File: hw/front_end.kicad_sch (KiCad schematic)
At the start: 6 parts, among them Q5 SSM6P35AFE, Q6 SSM6P35AFE

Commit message: WIP - a lot already laid out.
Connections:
- net FE_CHA/PGA_CTL_CLK: now also Q6.3 (D); no longer Q6.6 (D)
- net FE_CHA/PGA_CTL_DATA: now also Q5.6 (D); no longer Q6.3 (D)
- net FE_CHA/PGA_CTL_LATCH: now also Q6.6 (D); no longer Q5.3 (D)
- net FE_CHB/PGA_CTL_LATCH: now also Q5.3 (D); no longer Q5.6 (D)
- net PGA_LATCH_CHA: now also Q6.2 (G); no longer Q5.5 (G)
- net PGA_LATCH_CHB: now also Q5.5 (G); no longer Q5.2 (G)
- net PGA_SCLK: now also Q6.5 (G); no longer Q6.2 (G)
- net PGA_SDAT: now also Q5.2 (G); no longer Q6.5 (G)
- no-connect marks 2 -> 0
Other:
- sheet FE_CHA ports: added PGA_INLO, SE_OUT; removed none
- sheet FE_CHB ports: added PGA_INLO, SE_OUT; removed none
- moved on the sheet: Q5A, Q5B, Q6A, Q6B

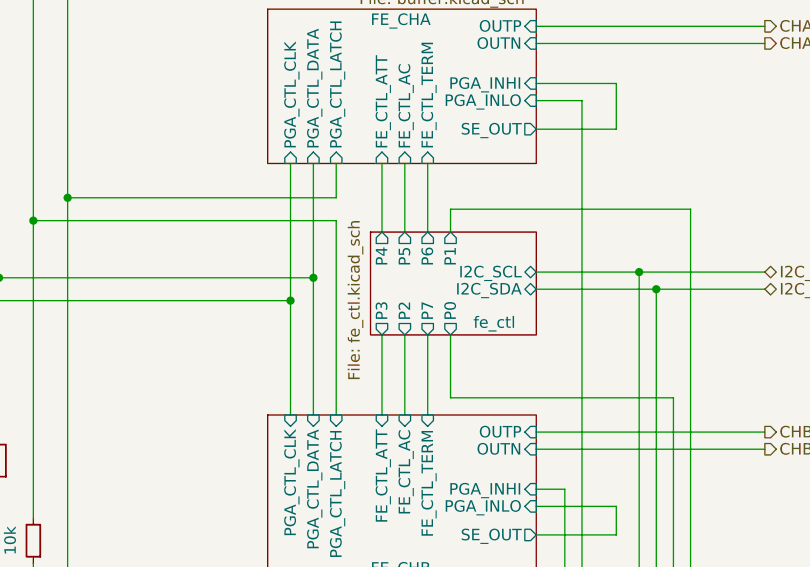
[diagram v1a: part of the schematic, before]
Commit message: WIP - almost everything except power (converters) connected
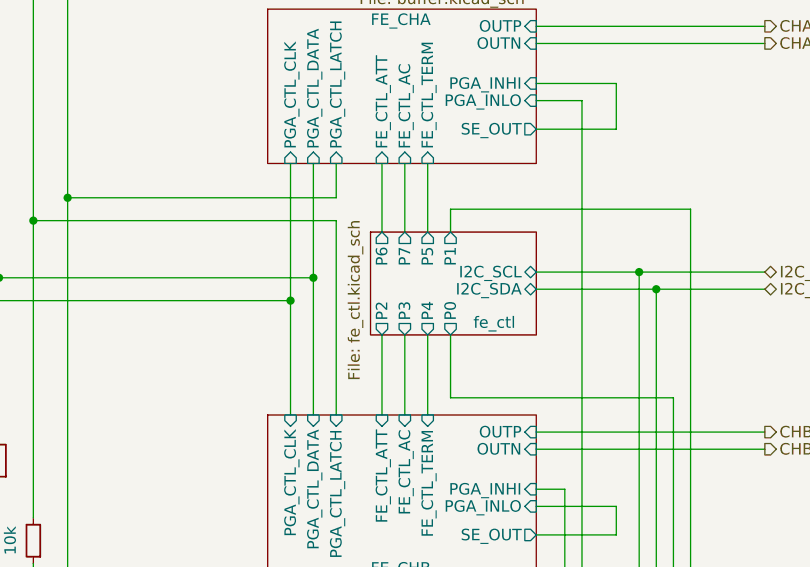
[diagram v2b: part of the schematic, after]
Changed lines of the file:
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@@
       (effects (font (size 1.27 1.27)) (justify left top))
     )
-    (pin "P7" output (at 111.125 113.03 270)
-      (effects (font (size 1.27 1.27)) (justify left))
+    (pin "P7" output (at 108.585 101.6 90)
+      (effects (font (size 1.27 1.27)) (justify right))
     )
     (pin "P0" output (at 113.665 113.03 270)
       (effects (font (size 1.27 1.27)) (justify left))
     )
-    (pin "P6" output (at 111.125 101.6 90)
+    (pin "P6" output (at 106.045 101.6 90)
       (effects (font (size 1.27 1.27)) (justify right))
     )
-    (pin "P5" output (at 108.585 101.6 90)
+    (pin "P5" output (at 111.125 101.6 90)
       (effects (font (size 1.27 1.27)) (justify right))
     )
-    (pin "P4" output (at 106.045 101.6 90)
-      (effects (font (size 1.27 1.27)) (justify right))
+    (pin "P4" output (at 111.125 113.03 270)
+      (effects (font (size 1.27 1.27)) (justify left))
     )
     (pin "P1" output (at 113.665 101.6 90)
       (effects (font (size 1.27 1.27)) (justify right))
     )
-    (pin "P2" output (at 108.585 113.03 270)
+    (pin "P2" output (at 106.045 113.03 270)
       (effects (font (size 1.27 1.27)) (justify left))
     )
-    (pin "P3" output (at 106.045 113.03 270)
+    (pin "P3" output (at 108.585 113.03 270)
       (effects (font (size 1.27 1.27)) (justify left))
     )

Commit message: finished routing; DRC passes (except for 1 hole violation at push-button)
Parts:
- Q5, Q6: Manufacturer (none) -> Toshiba; Part (none) -> SSM6P35AFE
- R23: Manufacturer Yageo -> (none); Part RT0603FRE0710KL -> (none)
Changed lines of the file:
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@@
+      (effects (font (size 1.27 1.27)) hide)
+    )
+    (property "Manufacturer" "Toshiba" (at 88.9 43.18 0)
+      (effects (font (size 1.27 1.27)) hide)
+    )
+    (property "Part" "SSM6P35AFE" (at 88.9 43.18 0)
       (effects (font (size 1.27 1.27)) hide)
     )
@@
       (effects (font (size 1.27 1.27)) hide)
     )
-    (property "Part" "RT0603FRE0710KL" (at 71.12 146.05 90)
-      (effects (font (size 1.27 1.27)) hide)
-    )
-    (property "Manufacturer" "Yageo" (at 71.12 146.05 90)
+    (property "Part" "" (at 71.12 146.05 90)
+      (effects (font (size 1.27 1.27)) hide)
+    )
+    (property "Manufacturer" "" (at 71.12 146.05 90)
       (effects (font (size 1.27 1.27)) hide)
     )
@@
       (effects (font (size 1.27 1.27)) hide)
     )
-    (property "Part" "RT0603FRE0710KL" (at 59.69 118.11 90)
-      (effects (font (size 1.27 1.27)) hide)
-    )
-    (property "Manufacturer" "Yageo" (at 59.69 118.11 90)
+    (property "Part" "" (at 59.69 118.11 90)
+      (effects (font (size 1.27 1.27)) hide)
+    )
+    (property "Manufacturer" "" (at 59.69 118.11 90)
       (effects (font (size 1.27 1.27)) hide)
     )
@@
     )
     (property "Datasheet" "~" (at 60.96 62.23 0)
+      (effects (font (size 1.27 1.27)) hide)
+    )
+    (property "Manufacturer" "Toshiba" (at 62.23 62.23 0)
+      (effects (font (size 1.27 1.27)) hide)
+    )
+    (property "Part" "SSM6P35AFE" (at 62.23 62.23 0)
       (effects (font (size 1.27 1.27)) hide)
     )
@@
       (effects (font (size 1.27 1.27)) hide)
     )
+    (property "Manufacturer" "Toshiba" (at 80.01 49.53 0)
+      (effects (font (size 1.27 1.27)) hide)
+    )
+    (property "Part" "SSM6P35AFE" (at 80.01 49.53 0)
+      (effects (font (size 1.27 1.27)) hide)
+    )
     (pin "1")
     (pin "2")
@@
       (effects (font (size 1.27 1.27)) hide)
     )
+    (property "Manufacturer" "Toshiba" (at 71.12 55.88 0)
+      (effects (font (size 1.27 1.27)) hide)
+    )
+    (property "Part" "SSM6P35AFE" (at 71.12 55.88 0)
+      (effects (font (size 1.27 1.27)) hide)
+    )
     (pin "1")
     (pin "2")
@@
       (effects (font (size 1.27 1.27)) hide)
     )
-    (property "Part" "RT0603FRE0710KL" (at 67.31 135.89 90)
-      (effects (font (size 1.27 1.27)) hide)
-    )
-    (property "Manufacturer" "Yageo" (at 67.31 135.89 90)
+    (property "Part" "" (at 67.31 135.89 90)
+      (effects (font (size 1.27 1.27)) hide)
+    )
+    (property "Manufacturer" "" (at 67.31 135.89 90)
       (effects (font (size 1.27 1.27)) hide)
     )
@@
       (effects (font (size 1.27 1.27)) hide)
     )
-    (property "Part" "RT0603FRE0710KL" (at 63.5 127 90)
-      (effects (font (size 1.27 1.27)) hide)
-    )
-    (property "Manufacturer" "Yageo" (at 63.5 127 90)
-      (effects (font (size 1.27 1.27)) hide)
-    )
+    (property "Part" "" (at 63.5 127 90)
+      (effects (font (size 1.27 1.27)) hide)
+    )
+    (property "Manufacturer" "" (at 63.5 127 90)
+      (effects (font (size 1.27 1.27)) hide)
+    )

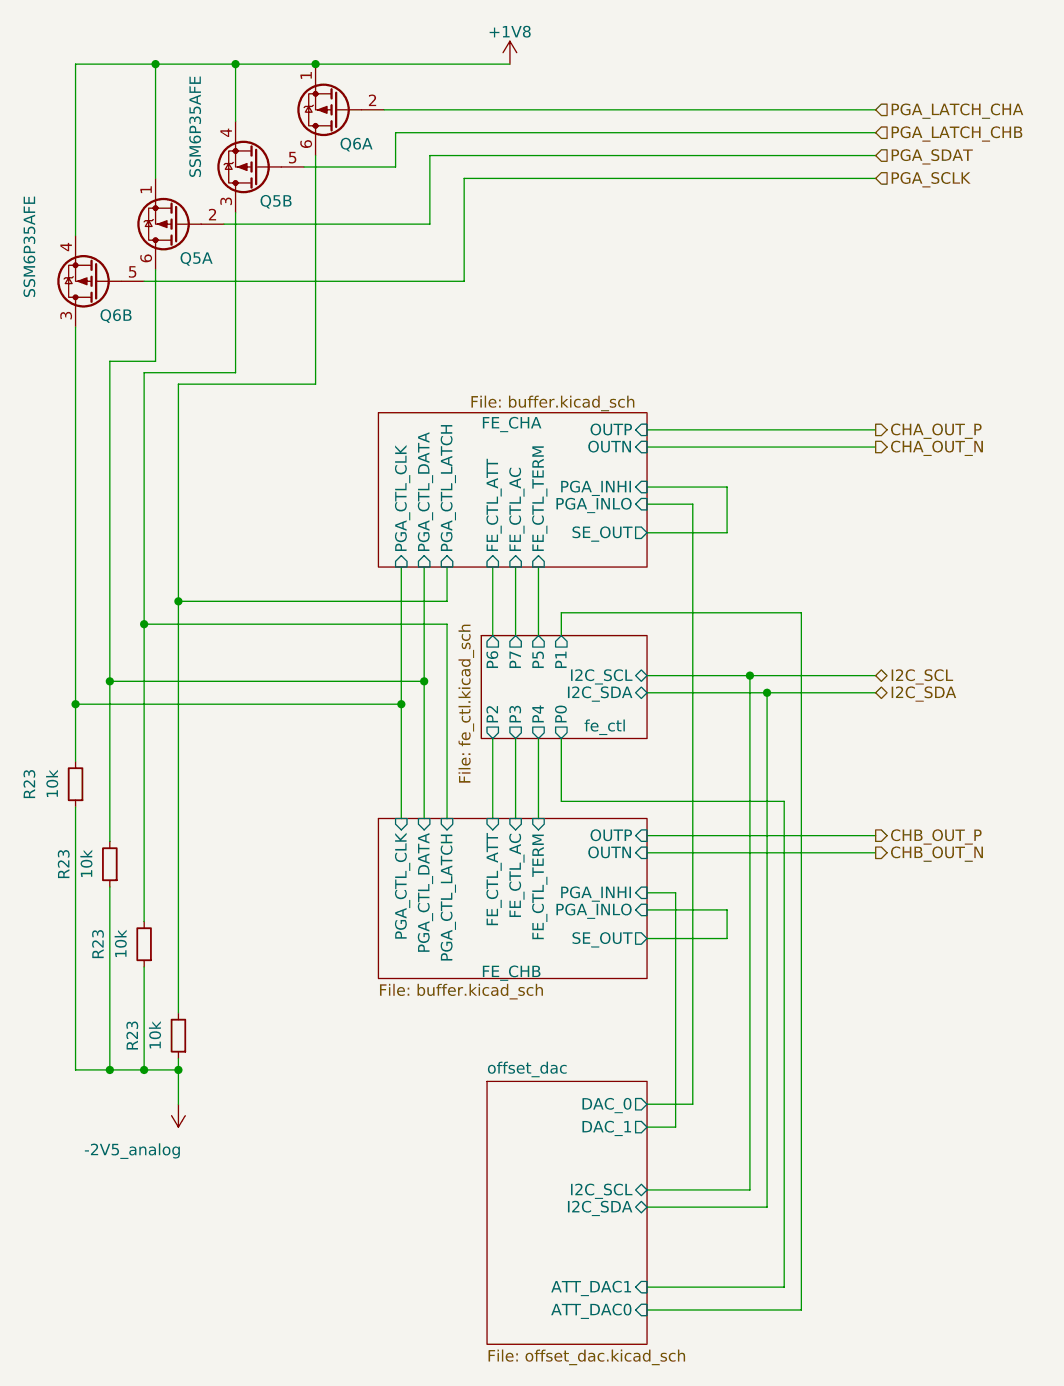
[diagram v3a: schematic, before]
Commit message: Added trion top-sheet as sub-sheet to usbadc project
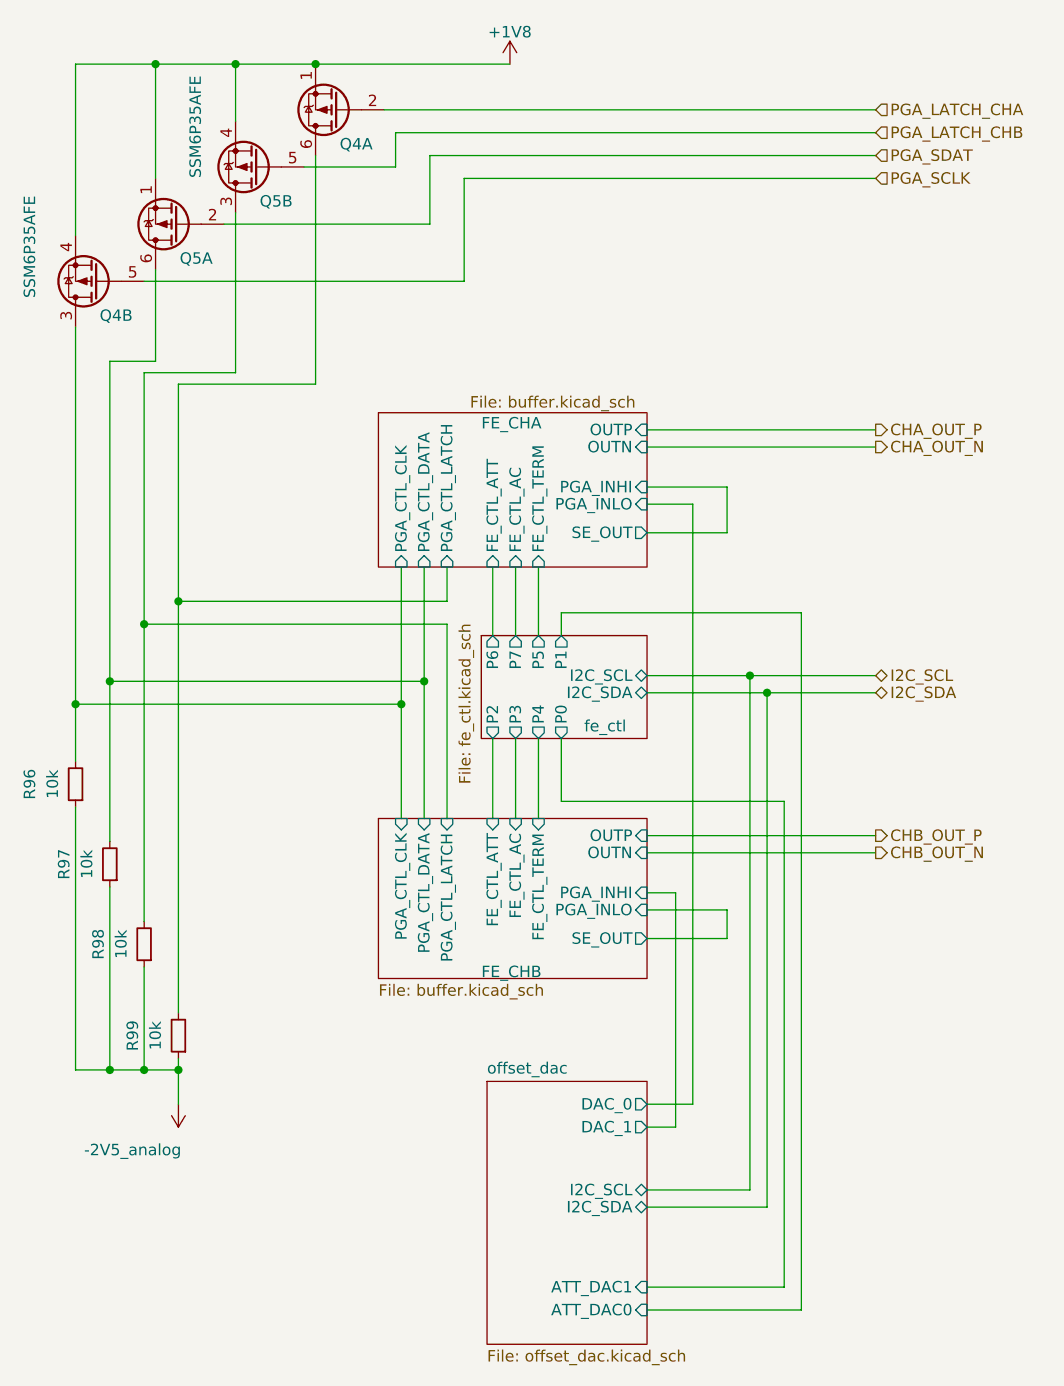
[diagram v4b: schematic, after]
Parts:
- renumbered Q6 to Q4, R23 to R96, R23 to R97, R23 to R98, R23 to R99
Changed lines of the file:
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@@
   (symbol (lib_id "Device:Q_Dual_PMOS_S1G1D2S2G2D1") (at 88.9 43.18 180) (unit 1)
     (in_bom yes) (on_board yes) (dnp no)
-    (property "Reference" "Q6" (at 92.71 46.99 0)
+    (property "Reference" "Q4" (at 92.71 46.99 0)
       (effects (font (size 1.27 1.27)) (justify left))
     )
@@
     (instances
       (project "usbadc"
-        (path "/7c8a1f8d-8834-4c9b-aaae-1f231e9b09a1/00000000-0000-0000-0000-0000612b1274"
-          (reference "Q6") (unit 1)
-        )
         (path "/7c8a1f8d-8834-4c9b-aaae-1f231e9b09a1/c969de1a-32a7-4770-b1aa-e527a627ef90"
           (reference "Q4") (unit 1)
@@
   (symbol (lib_id "Device:R_Small") (at 71.12 146.05 180) (unit 1)
     (in_bom yes) (on_board yes) (dnp no)
-    (property "Reference" "R23" (at 66.04 146.05 90)
+    (property "Reference" "R99" (at 66.04 146.05 90)
       (effects (font (size 1.27 1.27)))
     )
@@
     (instances
       (project "usbadc"
-        (path "/7c8a1f8d-8834-4c9b-aaae-1f231e9b09a1/00000000-0000-0000-0000-000060b16d71"
-          (reference "R23") (unit 1)
-        )
-        (path "/7c8a1f8d-8834-4c9b-aaae-1f231e9b09a1/00000000-0000-0000-0000-0000612b1274"
-          (reference "R100") (unit 1)
-        )
         (path "/7c8a1f8d-8834-4c9b-aaae-1f231e9b09a1/c969de1a-32a7-4770-b1aa-e527a627ef90"
           (reference "R99") (unit 1)
@@
   (symbol (lib_id "Device:R_Small") (at 59.69 118.11 180) (unit 1)
     (in_bom yes) (on_board yes) (dnp no)
-    (property "Reference" "R23" (at 54.61 118.11 90)
+    (property "Reference" "R96" (at 54.61 118.11 90)
       (effects (font (size 1.27 1.27)))
     )
@@
     (instances
       (project "usbadc"
-        (path "/7c8a1f8d-8834-4c9b-aaae-1f231e9b09a1/00000000-0000-0000-0000-000060b16d71"
-          (reference "R23") (unit 1)
-        )
-        (path "/7c8a1f8d-8834-4c9b-aaae-1f231e9b09a1/00000000-0000-0000-0000-0000612b1274"
-          (reference "R97") (unit 1)
-        )
         (path "/7c8a1f8d-8834-4c9b-aaae-1f231e9b09a1/c969de1a-32a7-4770-b1aa-e527a627ef90"
           (reference "R96") (unit 1)
@@
   (symbol (lib_id "Device:Q_Dual_PMOS_S1G1D2S2G2D1") (at 62.23 62.23 180) (unit 2)
     (in_bom yes) (on_board yes) (dnp no)
-    (property "Reference" "Q6" (at 66.04 66.04 0)
+    (property "Reference" "Q4" (at 66.04 66.04 0)
       (effects (font (size 1.27 1.27)) (justify left))
     )
@@
     (instances
       (project "usbadc"
-        (path "/7c8a1f8d-8834-4c9b-aaae-1f231e9b09a1/00000000-0000-0000-0000-0000612b1274"
-          (reference "Q6") (unit 2)
-        )
         (path "/7c8a1f8d-8834-4c9b-aaae-1f231e9b09a1/c969de1a-32a7-4770-b1aa-e527a627ef90"
           (reference "Q4") (unit 2)
@@
     (instances
       (project "usbadc"
-        (path "/7c8a1f8d-8834-4c9b-aaae-1f231e9b09a1/00000000-0000-0000-0000-0000612b1274"
+        (path "/7c8a1f8d-8834-4c9b-aaae-1f231e9b09a1/c969de1a-32a7-4770-b1aa-e527a627ef90"
           (reference "Q5") (unit 2)
         )
-        (path "/7c8a1f8d-8834-4c9b-aaae-1f231e9b09a1/c969de1a-32a7-4770-b1aa-e527a627ef90"
-          (reference "Q5") (unit 2)
-        )
       )
     )
@@
   (symbol (lib_id "fmc:-2V5_analog") (at 71.12 153.67 180) (unit 1)
     (in_bom yes) (on_board yes) (dnp no)
-    (property "Reference" "#PWR017" (at 71.12 149.86 0)
+    (property "Reference" "#PWR083" (at 71.12 149.86 0)
       (effects (font (size 1.27 1.27)) hide)
     )
@@
     (instances
       (project "usbadc"
-        (path "/7c8a1f8d-8834-4c9b-aaae-1f231e9b09a1/00000000-0000-0000-0000-00006086f2e3"
-          (reference "#PWR017") (unit 1)
-        )
-        (path "/7c8a1f8d-8834-4c9b-aaae-1f231e9b09a1/00000000-0000-0000-0000-0000612b1274"
-          (reference "#PWR025") (unit 1)
-        )
         (path "/7c8a1f8d-8834-4c9b-aaae-1f231e9b09a1/c969de1a-32a7-4770-b1aa-e527a627ef90"
           (reference "#PWR083") (unit 1)
@@
     (instances
       (project "usbadc"
-        (path "/7c8a1f8d-8834-4c9b-aaae-1f231e9b09a1/00000000-0000-0000-0000-0000612b1274"
+        (path "/7c8a1f8d-8834-4c9b-aaae-1f231e9b09a1/c969de1a-32a7-4770-b1aa-e527a627ef90"
           (reference "Q5") (unit 1)
         )
-        (path "/7c8a1f8d-8834-4c9b-aaae-1f231e9b09a1/c969de1a-32a7-4770-b1aa-e527a627ef90"
-          (reference "Q5") (unit 1)
-        )
       )
     )
@@
   (symbol (lib_id "Device:R_Small") (at 67.31 135.89 180) (unit 1)
     (in_bom yes) (on_board yes) (dnp no)
-    (property "Reference" "R23" (at 62.23 135.89 90)
+    (property "Reference" "R98" (at 62.23 135.89 90)
       (effects (font (size 1.27 1.27)))
     )
@@
     (instances
       (project "usbadc"
-        (path "/7c8a1f8d-8834-4c9b-aaae-1f231e9b09a1/00000000-0000-0000-0000-000060b16d71"
-          (reference "R23") (unit 1)
-        )
-        (path "/7c8a1f8d-8834-4c9b-aaae-1f231e9b09a1/00000000-0000-0000-0000-0000612b1274"
-          (reference "R99") (unit 1)
-        )
         (path "/7c8a1f8d-8834-4c9b-aaae-1f231e9b09a1/c969de1a-32a7-4770-b1aa-e527a627ef90"
           (reference "R98") (unit 1)
@@
   (symbol (lib_id "power:+1V8") (at 107.95 38.1 0) (unit 1)
     (in_bom yes) (on_board yes) (dnp no)
-    (property "Reference" "#PWR037" (at 107.95 41.91 0)
+    (property "Reference" "#PWR084" (at 107.95 41.91 0)
       (effects (font (size 1.27 1.27)) hide)
     )
@@
     (instances
       (project "usbadc"
-        (path "/7c8a1f8d-8834-4c9b-aaae-1f231e9b09a1/00000000-0000-0000-0000-0000612b1274"
-          (reference "#PWR037") (unit 1)
-        )
-        (path "/7c8a1f8d-8834-4c9b-aaae-1f231e9b09a1/00000000-0000-0000-0000-000060b16d71"
-          (reference "#PWR?") (unit 1)
-        )
-        (path "/7c8a1f8d-8834-4c9b-aaae-1f231e9b09a1/00000000-0000-0000-0000-00006086f2e3"
-          (reference "#PWR?") (unit 1)
-        )
         (path "/7c8a1f8d-8834-4c9b-aaae-1f231e9b09a1/c969de1a-32a7-4770-b1aa-e527a627ef90"
           (reference "#PWR084") (unit 1)
@@
   (symbol (lib_id "Device:R_Small") (at 63.5 127 180) (unit 1)
     (in_bom yes) (on_board yes) (dnp no)
-    (property "Reference" "R23" (at 58.42 127 90)
+    (property "Reference" "R97" (at 58.42 127 90)
       (effects (font (size 1.27 1.27)))
     )
@@
     (instances
       (project "usbadc"
-        (path "/7c8a1f8d-8834-4c9b-aaae-1f231e9b09a1/00000000-0000-0000-0000-000060b16d71"
-          (reference "R23") (unit 1)
-        )
-        (path "/7c8a1f8d-8834-4c9b-aaae-1f231e9b09a1/00000000-0000-0000-0000-0000612b1274"
-          (reference "R98") (unit 1)
-        )
         (path "/7c8a1f8d-8834-4c9b-aaae-1f231e9b09a1/c969de1a-32a7-4770-b1aa-e527a627ef90"
           (reference "R97") (unit 1)

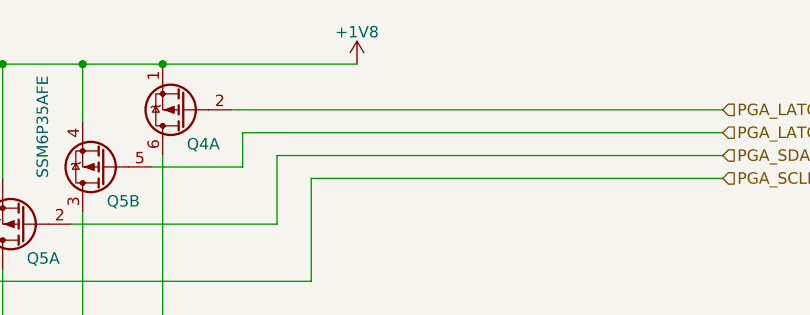
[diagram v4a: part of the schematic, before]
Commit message: rewired 1V8_analog to +2V5_analog
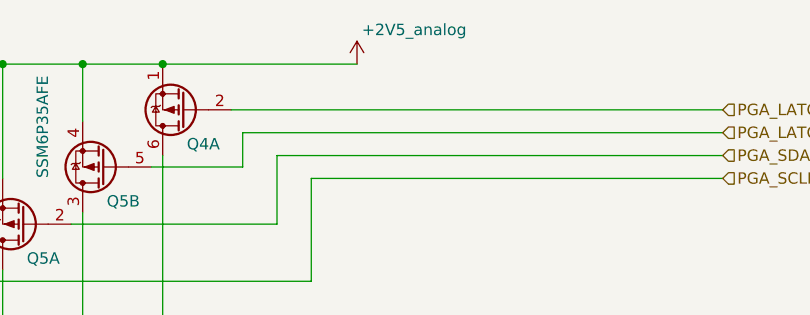
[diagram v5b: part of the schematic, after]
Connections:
- net +1V8 renamed +2V5_analog
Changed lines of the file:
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@@
+    )
+  )
+  (symbol (lib_id "fmc:+2V5_analog") (at 107.95 38.1 0) (unit 1)
+    (in_bom yes) (on_board yes) (dnp no)
+    (property "Reference" "#PWR088" (at 107.95 41.91 0)
+      (effects (font (size 1.27 1.27)) hide)
+    )
+    (property "Value" "+2V5_analog" (at 114.3 34.29 0)
+      (effects (font (size 1.27 1.27)))
+    )
+    (property "Footprint" "" (at 107.95 38.1 0)
+      (effects (font (size 1.27 1.27)) hide)
+    )
+    (property "Datasheet" "" (at 107.95 38.1 0)
+      (effects (font (size 1.27 1.27)) hide)
+    )
+    (pin "1")
+    (instances
+      (project "usbadc"
+        (path "/7c8a1f8d-8834-4c9b-aaae-1f231e9b09a1/c969de1a-32a7-4770-b1aa-e527a627ef90"
+          (reference "#PWR088") (unit 1)
+        )
+      )
     )
   )
@@
         )
       )
-    )
-  )
-  (symbol (lib_id "power:+1V8") (at 107.95 38.1 0) (unit 1)
-    (in_bom yes) (on_board yes) (dnp no)
-    (property "Reference" "#PWR084" (at 107.95 41.91 0)
-      (effects (font (size 1.27 1.27)) hide)
-    )
-    (property "Value" "+1V8" (at 107.95 34.544 0)
-      (effects (font (size 1.27 1.27)))
-    )
-    (property "Footprint" "" (at 107.95 38.1 0)
-      (effects (font (size 1.27 1.27)) hide)
-    )
-    (property "Datasheet" "" (at 107.95 38.1 0)
-      (effects (font (size 1.27 1.27)) hide)
-    )
-    (pin "1")
-    (instances
-      (project "usbadc"
-        (path "/7c8a1f8d-8834-4c9b-aaae-1f231e9b09a1/c969de1a-32a7-4770-b1aa-e527a627ef90"
-          (reference "#PWR084") (unit 1)
-        )
-      )
